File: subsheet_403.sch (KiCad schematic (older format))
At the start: 43 parts, among them Q404 2N3904, Q405 2N3904, U403 MC1377_COLOR_TELEVISION_RGB_T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

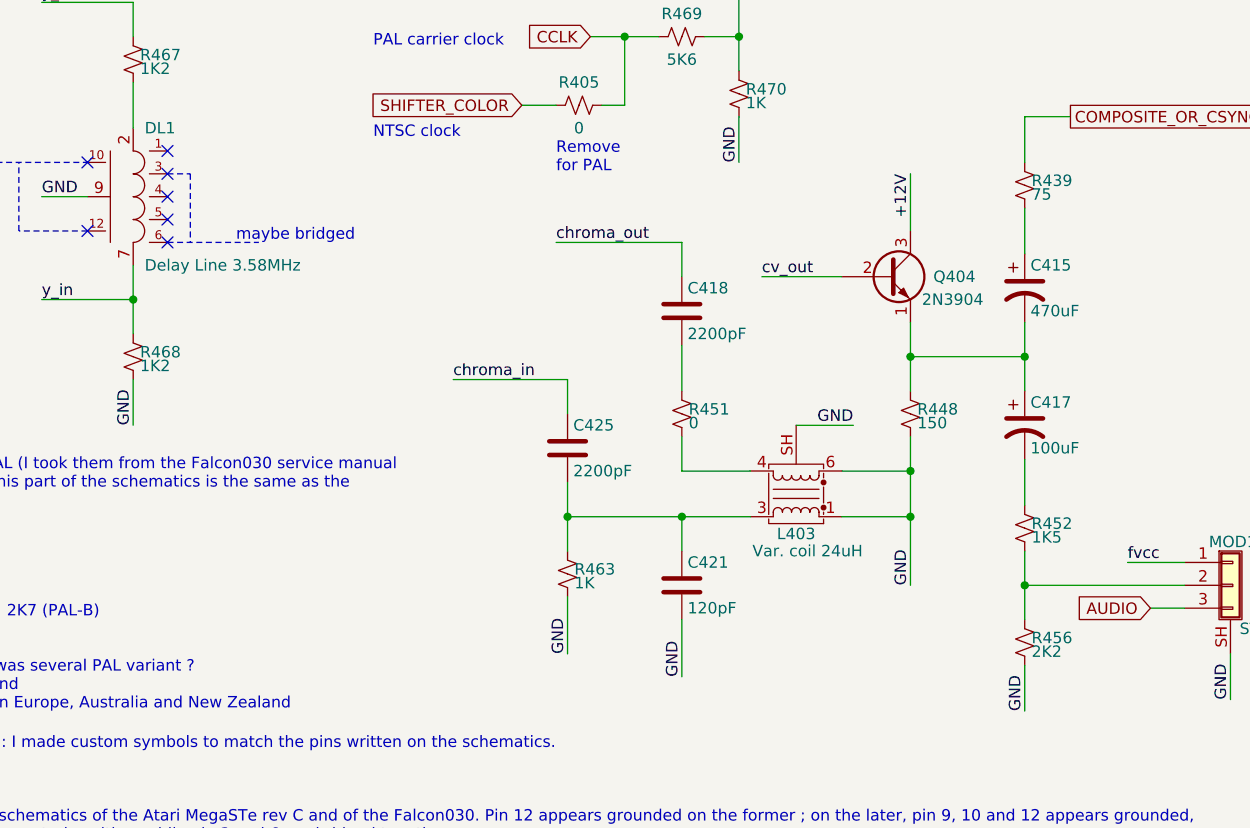
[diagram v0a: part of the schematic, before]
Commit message: [Schematics] bridged delay lines pins 3 and 6 to match pcb, fixed forgotten R442
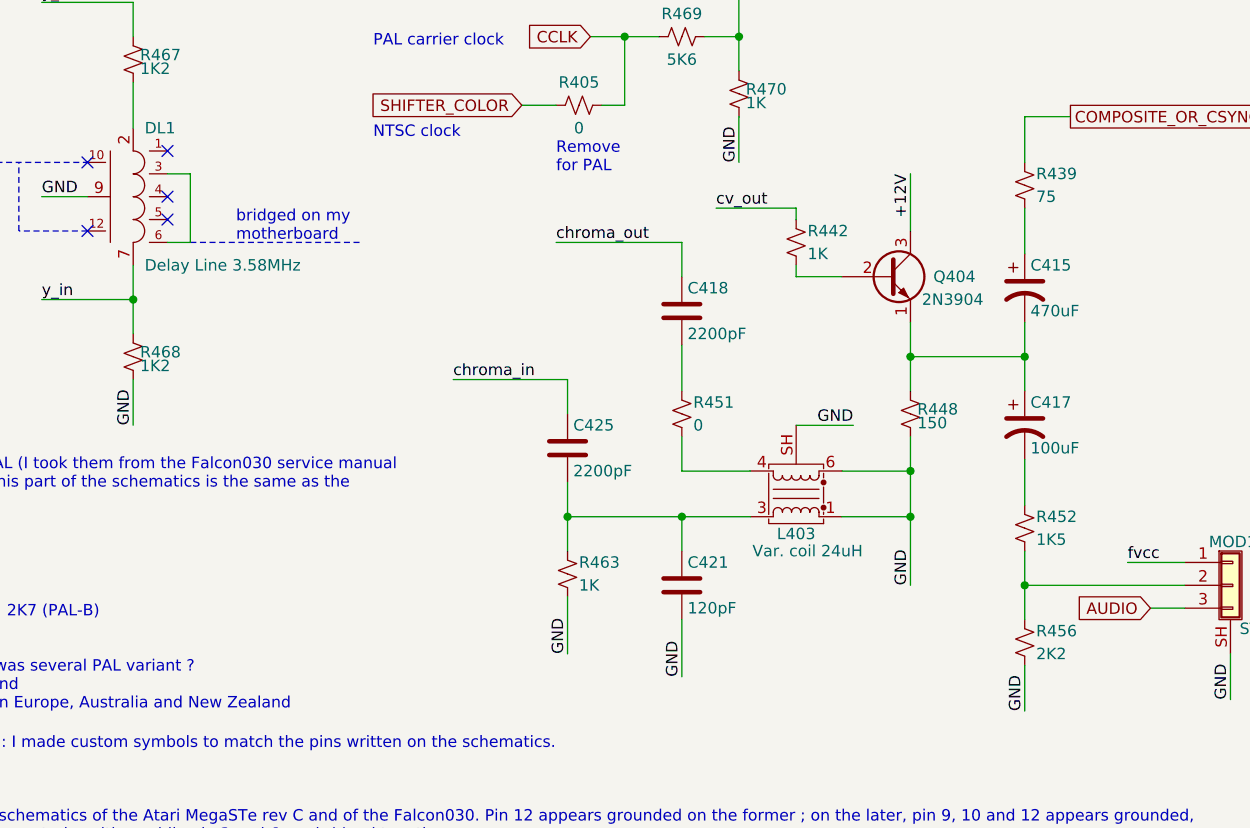
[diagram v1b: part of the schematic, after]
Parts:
- added R442: 1K, commons_passives_THT:Passive_THT_resistor_W2.54mm_L12.70mm, symbol Device:R_Small_US
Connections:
- net cv_out: now also R442.1; no longer Q404.2 (B)
- net at DL1.3: now also DL1.6
- new net: Q404.2 (B), R442.2
- no-connect marks 8 -> 6
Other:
- note added: "bridged on my \nmotherboard"
- note removed: "maybe bridged"
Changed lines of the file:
@@
 	1    0    0    -1
 $EndComp
-Text Label 4750 6700 0    50   ~ 0
+Text Label 4550 6400 0    50   ~ 0
 cv_out
 Text Label 5400 6250 3    50   ~ 0
@@
 AR Path="/60B3D9E3/60BDE5CE" Ref="R?"  Part="1"
 AR Path="/60B8B7AD/60BDE5CE" Ref="R439"  Part="1"
-F 0 "R439" H 5930 6320 50  0000 L CNN
-F 1 "75" H 5930 6260 50  0000 L CNN
+F 0 "R439" H 5950 6350 50  0000 L CNN
+F 1 "75" H 5950 6250 50  0000 L CNN
 F 2 "commons_passives_THT:Passive_THT_resistor_W2.54mm_L12.70mm" H 5900 6300 50  0001 C CNN
 F 3 "~" H 5900 6300 50  0001 C CNN
@@
 AR Path="/60B3D9E3/60BDF9EB" Ref="R?"  Part="1"
 AR Path="/60B8B7AD/60BDF9EB" Ref="R452"  Part="1"
-F 0 "R452" H 5930 7820 50  0000 L CNN
-F 1 "1K5" H 5930 7760 50  0000 L CNN
+F 0 "R452" H 5950 7850 50  0000 L CNN
+F 1 "1K5" H 5950 7750 50  0000 L CNN
 F 2 "commons_passives_THT:Passive_THT_resistor_W2.54mm_L12.70mm" H 5900 7800 50  0001 C CNN
 F 3 "~" H 5900 7800 50  0001 C CNN
@@
 AR Path="/60B3D9E3/60BE020F" Ref="R?"  Part="1"
 AR Path="/60B8B7AD/60BE020F" Ref="R456"  Part="1"
-F 0 "R456" H 5930 8320 50  0000 L CNN
-F 1 "2K2" H 5930 8260 50  0000 L CNN
+F 0 "R456" H 5950 8350 50  0000 L CNN
+F 1 "2K2" H 5950 8250 50  0000 L CNN
 F 2 "commons_passives_THT:Passive_THT_resistor_W2.54mm_L12.70mm" H 5900 8300 50  0001 C CNN
 F 3 "~" H 5900 8300 50  0001 C CNN
@@
 VCC
 Wire Wire Line
-	4750 6700 5100 6700
-Wire Wire Line
 	4400 8200 4400 8450
 Wire Wire Line
@@
 AR Path="/60B3D9E3/60C419C4" Ref="R?"  Part="1"
 AR Path="/60B8B7AD/60C419C4" Ref="R463"  Part="1"
-F 0 "R463" H 3930 8020 50  0000 L CNN
-F 1 "1K" H 3930 7960 50  0000 L CNN
+F 0 "R463" H 3950 8050 50  0000 L CNN
+F 1 "1K" H 3950 7950 50  0000 L CNN
 F 2 "commons_passives_THT:Passive_THT_resistor_W2.54mm_L12.70mm" H 3900 8000 50  0001 C CNN
 F 3 "~" H 3900 8000 50  0001 C CNN
@@
 AR Path="/60B3D9E3/60C370A7" Ref="R?"  Part="1"
 AR Path="/60B8B7AD/60C370A7" Ref="R451"  Part="1"
-F 0 "R451" H 4430 7320 50  0000 L CNN
-F 1 "0" H 4430 7260 50  0000 L CNN
+F 0 "R451" H 4450 7350 50  0000 L CNN
+F 1 "0" H 4450 7250 50  0000 L CNN
 F 2 "commons_passives_THT:Passive_THT_resistor_W2.54mm_L12.70mm" H 4400 7300 50  0001 C CNN
 F 3 "~" H 4400 7300 50  0001 C CNN
@@
 NoConn ~ 1800 6500
 NoConn ~ 2150 6150
-NoConn ~ 2150 6250
 NoConn ~ 2150 6350
 NoConn ~ 2150 6450
-NoConn ~ 2150 6550
 Text Notes 750  6200 0    50   ~ 0
 maybe grounded
@@
 Wire Notes Line
 	1500 6500 1500 6200
-Wire Notes Line
-	2150 6250 2250 6250
-Wire Notes Line
-	2250 6250 2250 6550
 Text Notes 2450 6550 0    50   ~ 0
-maybe bridged
+bridged on my \nmotherboard
 Wire Notes Line
 	1150 6200 1800 6200
-Wire Notes Line
-	2150 6550 2550 6550
 Connection ~ 4650 5650
 Wire Wire Line
@@
 Text Label 5150 7350 2    50   ~ 0
 GND
+Wire Wire Line
+	2150 6250 2250 6250
+Wire Wire Line
+	2250 6250 2250 6550
+Wire Wire Line
+	2250 6550 2150 6550
+Wire Notes Line
+	2250 6550 3000 6550
+$Comp
+L Device:R_Small_US R?
+U 1 1 610EC475
+P 4900 6550
+AR Path="/60B3D9E3/610EC475" Ref="R?"  Part="1"
+AR Path="/60B8B7AD/610EC475" Ref="R442"  Part="1"
+F 0 "R442" H 4950 6600 50  0000 L CNN
+F 1 "1K" H 4950 6500 50  0000 L CNN
+F 2 "commons_passives_THT:Passive_THT_resistor_W2.54mm_L12.70mm" H 4900 6550 50  0001 C CNN
+F 3 "~" H 4900 6550 50  0001 C CNN
+	1    4900 6550
+	1    0    0    -1
+$EndComp
+Wire Wire Line
+	4900 6650 4900 6700
+Wire Wire Line
+	4900 6700 5100 6700
+Wire Wire Line
+	4550 6400 4900 6400
+Wire Wire Line
+	4900 6400 4900 6450
 $EndSCHEMATC
